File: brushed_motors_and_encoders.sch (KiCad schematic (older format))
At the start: 23 parts, among them J301 M0_CONN, J302 M1_CONN, J303 M2_CONN, J304 M3_CONN, J309 External encoders power, J310 Encoder Commector, U301 DRV8871DDA, U302 DRV8871DDA, U303 DRV8871DDA, U304 DRV8871DDA

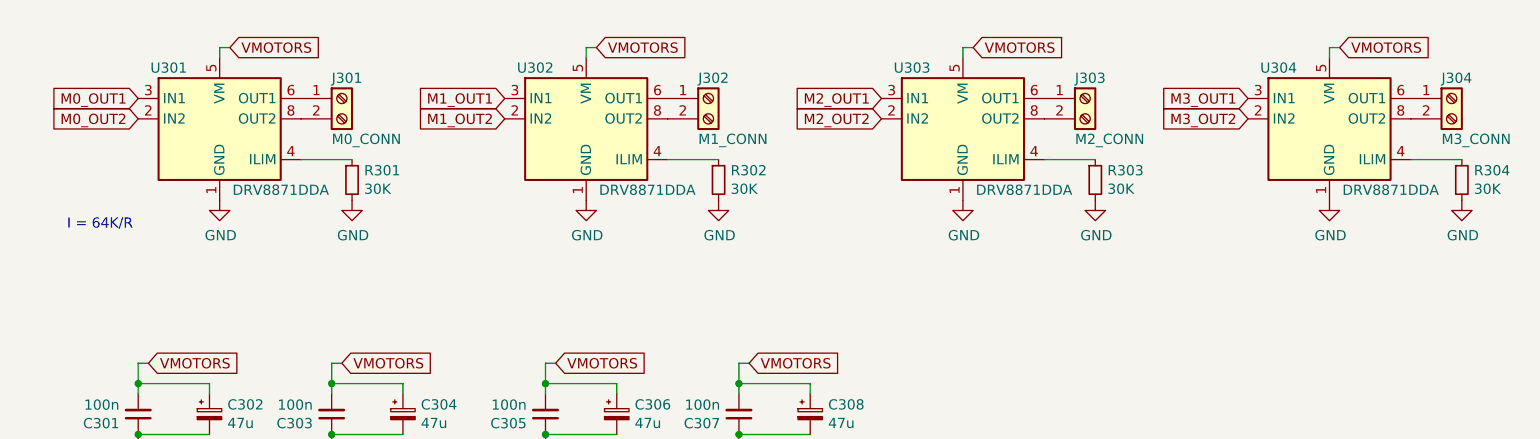
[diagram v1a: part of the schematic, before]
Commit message: Change footprint for a comonent
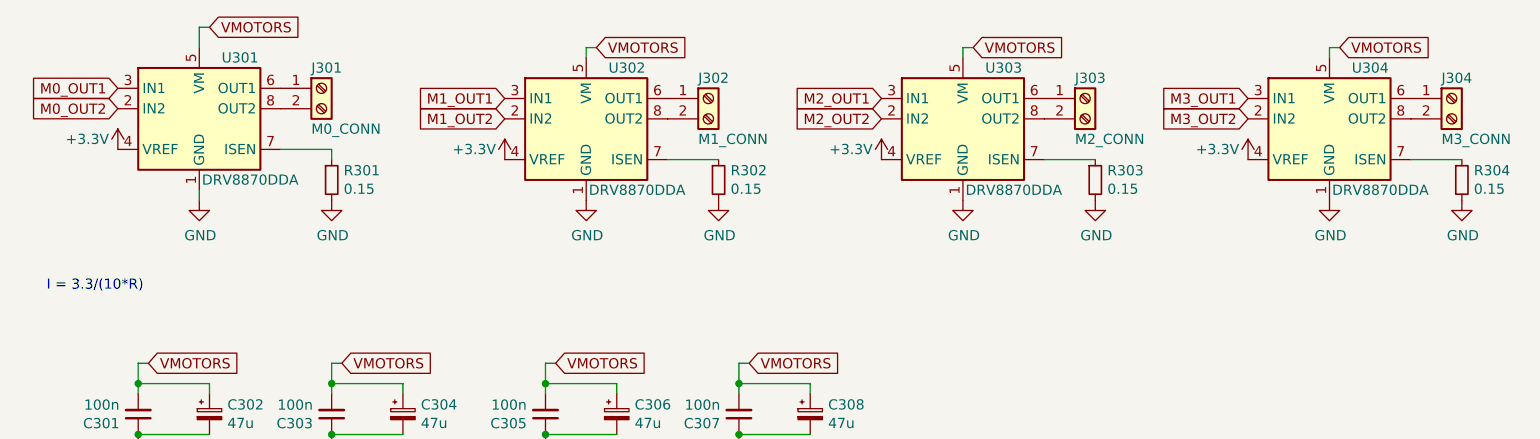
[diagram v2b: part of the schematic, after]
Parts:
- removed U301, U302, U303, U304: DRV8871DDA, Package_SO:Texas_HTSOP-8-1EP_3.9x4.9mm_P1.27mm_EP2.95x4.9mm_Mask2.4x3.1mm_ThermalVias, symbol Driver_Motor:DRV8871DDA
- added U301, U302, U303, U304: DRV8870DDA, Package_SO:Texas_HTSOP-8-1EP_3.9x4.9mm_P1.27mm_EP2.95x4.9mm_Mask2.4x3.1mm_ThermalVias, symbol Driver_Motor:DRV8870DDA
- R301, R302, R303, R304: value 30K -> 0.15; LCSC Part # C22984 -> C45879
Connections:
- net +3V3: now also U301.4 (VREF), U302.4 (VREF), U303.4 (VREF), U304.4 (VREF)
- net GND: now also U301.1 (GND), U301.9 (GND), U302.1 (GND), U302.9 (GND), U303.1 (GND), U303.9 (GND), U304.1 (GND), U304.9 (GND)
- net M0_OUT1: now also U301.3 (IN1)
- net M0_OUT2: now also U301.2 (IN2)
- net M1_OUT1: now also U302.3 (IN1)
- net M1_OUT2: now also U302.2 (IN2)
- net M2_OUT1: now also U303.3 (IN1)
- net M2_OUT2: now also U303.2 (IN2)
- net M3_OUT1: now also U304.3 (IN1)
- net M3_OUT2: now also U304.2 (IN2)
- net VMOTORS: now also U301.5 (VM), U302.5 (VM), U303.5 (VM), U304.5 (VM)
- net at R302.1: now also U302.7 (ISEN)
- net at J302.1 (Pin_1): now also U302.6 (OUT1)
- net at J302.2 (Pin_2): now also U302.8 (OUT2)
- net at R304.1: now also U304.7 (ISEN)
- net at J304.1 (Pin_1): now also U304.6 (OUT1)
- net at J304.2 (Pin_2): now also U304.8 (OUT2)
- net at R301.1: now also U301.7 (ISEN)
- net at J301.1 (Pin_1): now also U301.6 (OUT1)
- net at J301.2 (Pin_2): now also U301.8 (OUT2)
- net at R303.1: now also U303.7 (ISEN)
- net at J303.1 (Pin_1): now also U303.6 (OUT1)
- net at J303.2 (Pin_2): now also U303.8 (OUT2)
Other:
- note added: "I = 3.3/(10*R)"
- note removed: "I = 64K/R"
- moved on the sheet: J301, R301
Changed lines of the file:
@@
 Wire Wire Line
 	4900 1500 4850 1500
-$Comp
-L Driver_Motor:DRV8871DDA U?
-U 1 1 60A45ACD
-P 4850 1850
-AR Path="/60A45ACD" Ref="U?"  Part="1"
-AR Path="/60A3E5C0/60A45ACD" Ref="U302"  Part="1"
-F 0 "U302" H 4600 2100 50  0000 C CNN
-F 1 "DRV8871DDA" H 5150 1500 50  0000 C CNN
-F 2 "Package_SO:Texas_HTSOP-8-1EP_3.9x4.9mm_P1.27mm_EP2.95x4.9mm_Mask2.4x3.1mm_ThermalVias" H 5100 1800 50  0001 C CNN
-F 3 "http://www.ti.com/lit/ds/symlink/drv8871.pdf" H 5100 1800 50  0001 C CNN
-F 4 "C75864" H 4850 1850 50  0001 C CNN "LCSC Part #"
-	1    4850 1850
-	1    0    0    -1
-$EndComp
 Wire Wire Line
 	8500 1500 8500 1550
@@
 Text GLabel 6750 1500 2    50   Input ~ 0
 VMOTORS
-Text GLabel 3100 1500 2    50   Input ~ 0
-VMOTORS
-Wire Wire Line
-	3050 1500 3050 1550
-Wire Wire Line
-	3100 1500 3050 1500
+Text GLabel 3000 1400 2    50   Input ~ 0
+VMOTORS
 Text GLabel 4900 1500 2    50   Input ~ 0
 VMOTORS
-$Comp
-L Driver_Motor:DRV8871DDA U?
-U 1 1 60A45AEE
-P 8500 1850
-AR Path="/60A45AEE" Ref="U?"  Part="1"
-AR Path="/60A3E5C0/60A45AEE" Ref="U304"  Part="1"
-F 0 "U304" H 8250 2100 50  0000 C CNN
-F 1 "DRV8871DDA" H 8800 1500 50  0000 C CNN
-F 2 "Package_SO:Texas_HTSOP-8-1EP_3.9x4.9mm_P1.27mm_EP2.95x4.9mm_Mask2.4x3.1mm_ThermalVias" H 8750 1800 50  0001 C CNN
-F 3 "http://www.ti.com/lit/ds/symlink/drv8871.pdf" H 8750 1800 50  0001 C CNN
-F 4 "C75864" H 8500 1850 50  0001 C CNN "LCSC Part #"
-	1    8500 1850
-	1    0    0    -1
-$EndComp
 Wire Wire Line
 	8900 2050 9150 2050
@@
 AR Path="/60A3E5C0/60A45AFC" Ref="R304"  Part="1"
 F 0 "R304" H 9209 2196 50  0000 L CNN
-F 1 "30K" H 9209 2105 50  0000 L CNN
+F 1 "0.15" H 9209 2105 50  0000 L CNN
 F 2 "Resistor_SMD:R_0603_1608Metric" H 9150 2150 50  0001 C CNN
 F 3 "~" H 9150 2150 50  0001 C CNN
-F 4 "C22984" H 9150 2150 50  0001 C CNN "LCSC Part #"
+F 4 "C45879" H 9150 2150 50  0001 C CNN "LCSC Part #"
 	1    9150 2150
 	1    0    0    -1
@@
 Text GLabel 8100 1750 0    50   Input ~ 0
 M3_OUT1
-$Comp
-L Driver_Motor:DRV8871DDA U?
-U 1 1 60A45B11
-P 3050 1850
-AR Path="/60A45B11" Ref="U?"  Part="1"
-AR Path="/60A3E5C0/60A45B11" Ref="U301"  Part="1"
-F 0 "U301" H 2800 2100 50  0000 C CNN
-F 1 "DRV8871DDA" H 3350 1500 50  0000 C CNN
-F 2 "Package_SO:Texas_HTSOP-8-1EP_3.9x4.9mm_P1.27mm_EP2.95x4.9mm_Mask2.4x3.1mm_ThermalVias" H 3300 1800 50  0001 C CNN
-F 3 "http://www.ti.com/lit/ds/symlink/drv8871.pdf" H 3300 1800 50  0001 C CNN
-F 4 "C75864" H 3050 1850 50  0001 C CNN "LCSC Part #"
-	1    3050 1850
-	1    0    0    -1
-$EndComp
-Text Notes 2300 2400 0    50   ~ 0
-I = 64K/R
-$Comp
-L Driver_Motor:DRV8871DDA U?
-U 1 1 60A45B19
-P 6700 1850
-AR Path="/60A45B19" Ref="U?"  Part="1"
-AR Path="/60A3E5C0/60A45B19" Ref="U303"  Part="1"
-F 0 "U303" H 6450 2100 50  0000 C CNN
-F 1 "DRV8871DDA" H 7000 1500 50  0000 C CNN
-F 2 "Package_SO:Texas_HTSOP-8-1EP_3.9x4.9mm_P1.27mm_EP2.95x4.9mm_Mask2.4x3.1mm_ThermalVias" H 6950 1800 50  0001 C CNN
-F 3 "http://www.ti.com/lit/ds/symlink/drv8871.pdf" H 6950 1800 50  0001 C CNN
-F 4 "C75864" H 6700 1850 50  0001 C CNN "LCSC Part #"
-	1    6700 1850
-	1    0    0    -1
-$EndComp
+Text Notes 2200 2700 0    50   ~ 0
+I = 3.3/(10*R)
 Wire Wire Line
 	7100 2050 7350 2050
@@
 AR Path="/60A3E5C0/60A45B27" Ref="R303"  Part="1"
 F 0 "R303" H 7409 2196 50  0000 L CNN
-F 1 "30K" H 7409 2105 50  0000 L CNN
+F 1 "0.15" H 7409 2105 50  0000 L CNN
 F 2 "Resistor_SMD:R_0603_1608Metric" H 7350 2150 50  0001 C CNN
 F 3 "~" H 7350 2150 50  0001 C CNN
-F 4 "C22984" H 7350 2150 50  0001 C CNN "LCSC Part #"
+F 4 "C45879" H 7350 2150 50  0001 C CNN "LCSC Part #"
 	1    7350 2150
 	1    0    0    -1
@@
 AR Path="/60A3E5C0/60A45B43" Ref="R302"  Part="1"
 F 0 "R302" H 5559 2196 50  0000 L CNN
-F 1 "30K" H 5559 2105 50  0000 L CNN
+F 1 "0.15" H 5559 2105 50  0000 L CNN
 F 2 "Resistor_SMD:R_0603_1608Metric" H 5500 2150 50  0001 C CNN
 F 3 "~" H 5500 2150 50  0001 C CNN
-F 4 "C22984" H 5500 2150 50  0001 C CNN "LCSC Part #"
+F 4 "C45879" H 5500 2150 50  0001 C CNN "LCSC Part #"
 	1    5500 2150
 	1    0    0    -1
@@
 L power:GND #PWR?
 U 1 1 60A45BB7
-P 3700 2250
+P 3600 2250
 AR Path="/60A45BB7" Ref="#PWR?"  Part="1"
 AR Path="/60A3E5C0/60A45BB7" Ref="#PWR0304"  Part="1"
-F 0 "#PWR0304" H 3700 2000 50  0001 C CNN
-F 1 "GND" H 3705 2077 50  0000 C CNN
-F 2 "" H 3700 2250 50  0001 C CNN
-F 3 "" H 3700 2250 50  0001 C CNN
-	1    3700 2250
-	1    0    0    -1
-$EndComp
-Wire Wire Line
-	3450 2050 3700 2050
+F 0 "#PWR0304" H 3600 2000 50  0001 C CNN
+F 1 "GND" H 3605 2077 50  0000 C CNN
+F 2 "" H 3600 2250 50  0001 C CNN
+F 3 "" H 3600 2250 50  0001 C CNN
+	1    3600 2250
+	1    0    0    -1
+$EndComp
 $Comp
 L Device:R_Small R?
 U 1 1 60A45BBF
-P 3700 2150
+P 3600 2150
 AR Path="/60A45BBF" Ref="R?"  Part="1"
 AR Path="/60A3E5C0/60A45BBF" Ref="R301"  Part="1"
-F 0 "R301" H 3759 2196 50  0000 L CNN
-F 1 "30K" H 3759 2105 50  0000 L CNN
-F 2 "Resistor_SMD:R_0603_1608Metric" H 3700 2150 50  0001 C CNN
-F 3 "~" H 3700 2150 50  0001 C CNN
-F 4 "C22984" H 3700 2150 50  0001 C CNN "LCSC Part #"
-	1    3700 2150
+F 0 "R301" H 3659 2196 50  0000 L CNN
+F 1 "0.15" H 3659 2105 50  0000 L CNN
+F 2 "Resistor_SMD:R_0603_1608Metric" H 3600 2150 50  0001 C CNN
+F 3 "~" H 3600 2150 50  0001 C CNN
+F 4 "C45879" H 3600 2150 50  0001 C CNN "LCSC Part #"
+	1    3600 2150
 	1    0    0    -1
 $EndComp
@@
 L Connector:Screw_Terminal_01x02 J?
 U 1 1 60A45BC5
-P 3650 1750
+P 3550 1700
 AR Path="/60A45BC5" Ref="J?"  Part="1"
 AR Path="/60A3E5C0/60A45BC5" Ref="J301"  Part="1"
-F 0 "J301" H 3600 1850 50  0000 L CNN
-F 1 "M0_CONN" H 3600 1550 50  0000 L CNN
-F 2 "VsReality_Footprints:Ningbo_Kangnex_Elec_WJ128V_5_0_2P" H 3650 1750 50  0001 C CNN
-F 3 "~" H 3650 1750 50  0001 C CNN
-	1    3650 1750
-	1    0    0    -1
-$EndComp
-Text GLabel 2650 1850 0    50   Input ~ 0
+F 0 "J301" H 3500 1800 50  0000 L CNN
+F 1 "M0_CONN" H 3500 1500 50  0000 L CNN
+F 2 "VsReality_Footprints:Ningbo_Kangnex_Elec_WJ128V_5_0_2P" H 3550 1700 50  0001 C CNN
+F 3 "~" H 3550 1700 50  0001 C CNN
+	1    3550 1700
+	1    0    0    -1
+$EndComp
+Text GLabel 2550 1800 0    50   Input ~ 0
 M0_OUT2
-Text GLabel 2650 1750 0    50   Input ~ 0
+Text GLabel 2550 1700 0    50   Input ~ 0
 M0_OUT1
 $Comp
 L power:GND #PWR?
 U 1 1 60A45BCD
-P 3050 2250
+P 2950 2250
 AR Path="/60A45BCD" Ref="#PWR?"  Part="1"
 AR Path="/60A3E5C0/60A45BCD" Ref="#PWR0303"  Part="1"
-F 0 "#PWR0303" H 3050 2000 50  0001 C CNN
-F 1 "GND" H 3055 2077 50  0000 C CNN
-F 2 "" H 3050 2250 50  0001 C CNN
-F 3 "" H 3050 2250 50  0001 C CNN
-	1    3050 2250
+F 0 "#PWR0303" H 2950 2000 50  0001 C CNN
+F 1 "GND" H 2955 2077 50  0000 C CNN
+F 2 "" H 2950 2250 50  0001 C CNN
+F 3 "" H 2950 2250 50  0001 C CNN
+	1    2950 2250
 	1    0    0    -1
 $EndComp
@@
 	1    0    0    1
 $EndComp
+$Comp
+L Driver_Motor:DRV8870DDA U301
+U 1 1 62347C0E
+P 2950 1800
+F 0 "U301" H 3150 2050 50  0000 C CNN
+F 1 "DRV8870DDA" H 3200 1450 50  0000 C CNN
+F 2 "Package_SO:Texas_HTSOP-8-1EP_3.9x4.9mm_P1.27mm_EP2.95x4.9mm_Mask2.4x3.1mm_ThermalVias" H 3050 1700 50  0001 C CNN
+F 3 "http://www.ti.com/lit/ds/symlink/drv8870.pdf" H 2700 2150 50  0001 C CNN
+F 4 "C86590" H 2950 1800 50  0001 C CNN "LCSC Part #"
+	1    2950 1800
+	1    0    0    -1
+$EndComp
+Wire Wire Line
+	3000 1400 2950 1400
+Wire Wire Line
+	2950 1400 2950 1500
+$Comp
+L power:+3.3V #PWR0314
+U 1 1 6234FC60
+P 4450 2050
+F 0 "#PWR0314" H 4450 1900 50  0001 C CNN
+F 1 "+3.3V" H 4300 2100 50  0000 C CNN
+F 2 "" H 4450 2050 50  0001 C CNN
+F 3 "" H 4450 2050 50  0001 C CNN
+	1    4450 2050
+	1    0    0    -1
+$EndComp
+Wire Wire Line
+	3350 2000 3600 2000
+Wire Wire Line
+	3600 2000 3600 2050
+Wire Wire Line
+	2950 2200 2950 2250
+$Comp
+L Driver_Motor:DRV8870DDA U302
+U 1 1 6235CDC4
+P 4850 1850
+F 0 "U302" H 5050 2100 50  0000 C CNN
+F 1 "DRV8870DDA" H 5100 1500 50  0000 C CNN
+F 2 "Package_SO:Texas_HTSOP-8-1EP_3.9x4.9mm_P1.27mm_EP2.95x4.9mm_Mask2.4x3.1mm_ThermalVias" H 4950 1750 50  0001 C CNN
+F 3 "http://www.ti.com/lit/ds/symlink/drv8870.pdf" H 4600 2200 50  0001 C CNN
+F 4 "C86590" H 4850 1850 50  0001 C CNN "LCSC Part #"
+	1    4850 1850
+	1    0    0    -1
+$EndComp
+$Comp
+L Driver_Motor:DRV8870DDA U303
+U 1 1 6235E3DF
+P 6700 1850
+F 0 "U303" H 6900 2100 50  0000 C CNN
+F 1 "DRV8870DDA" H 6950 1500 50  0000 C CNN
+F 2 "Package_SO:Texas_HTSOP-8-1EP_3.9x4.9mm_P1.27mm_EP2.95x4.9mm_Mask2.4x3.1mm_ThermalVias" H 6800 1750 50  0001 C CNN
+F 3 "http://www.ti.com/lit/ds/symlink/drv8870.pdf" H 6450 2200 50  0001 C CNN
+F 4 "C86590" H 6700 1850 50  0001 C CNN "LCSC Part #"
+	1    6700 1850
+	1    0    0    -1
+$EndComp
+$Comp
+L Driver_Motor:DRV8870DDA U304
+U 1 1 6235EBDB
+P 8500 1850
+F 0 "U304" H 8700 2100 50  0000 C CNN
+F 1 "DRV8870DDA" H 8750 1500 50  0000 C CNN
+F 2 "Package_SO:Texas_HTSOP-8-1EP_3.9x4.9mm_P1.27mm_EP2.95x4.9mm_Mask2.4x3.1mm_ThermalVias" H 8600 1750 50  0001 C CNN
+F 3 "http://www.ti.com/lit/ds/symlink/drv8870.pdf" H 8250 2200 50  0001 C CNN
+F 4 "C86590" H 8500 1850 50  0001 C CNN "LCSC Part #"
+	1    8500 1850
+	1    0    0    -1
+$EndComp
+$Comp
+L power:+3.3V #PWR0313
+U 1 1 62365411
+P 2550 2000
+F 0 "#PWR0313" H 2550 1850 50  0001 C CNN
+F 1 "+3.3V" H 2400 2050 50  0000 C CNN
+F 2 "" H 2550 2000 50  0001 C CNN
+F 3 "" H 2550 2000 50  0001 C CNN
+	1    2550 2000
+	1    0    0    -1
+$EndComp
+$Comp
+L power:+3.3V #PWR0315
+U 1 1 623657B3
+P 6300 2050
+F 0 "#PWR0315" H 6300 1900 50  0001 C CNN
+F 1 "+3.3V" H 6150 2100 50  0000 C CNN
+F 2 "" H 6300 2050 50  0001 C CNN
+F 3 "" H 6300 2050 50  0001 C CNN
+	1    6300 2050
+	1    0    0    -1
+$EndComp
+$Comp
+L power:+3.3V #PWR0316
+U 1 1 62365C61
+P 8100 2050
+F 0 "#PWR0316" H 8100 1900 50  0001 C CNN
+F 1 "+3.3V" H 7950 2100 50  0000 C CNN
+F 2 "" H 8100 2050 50  0001 C CNN
+F 3 "" H 8100 2050 50  0001 C CNN
+	1    8100 2050
+	1    0    0    -1
+$EndComp
 $EndSCHEMATC
